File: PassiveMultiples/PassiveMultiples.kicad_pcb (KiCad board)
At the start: 2 copper layers, 15 x 100 mm, 9 parts, among them J1 AudioJack2_SwitchT, J2 AudioJack2_SwitchT, J3 AudioJack2_SwitchT, J4 AudioJack2_SwitchT, J5 AudioJack2_SwitchT, J6 AudioJack2_SwitchT, J7 AudioJack2_SwitchT, J8 AudioJack2_SwitchT, SW1 SW_Push_DPDT

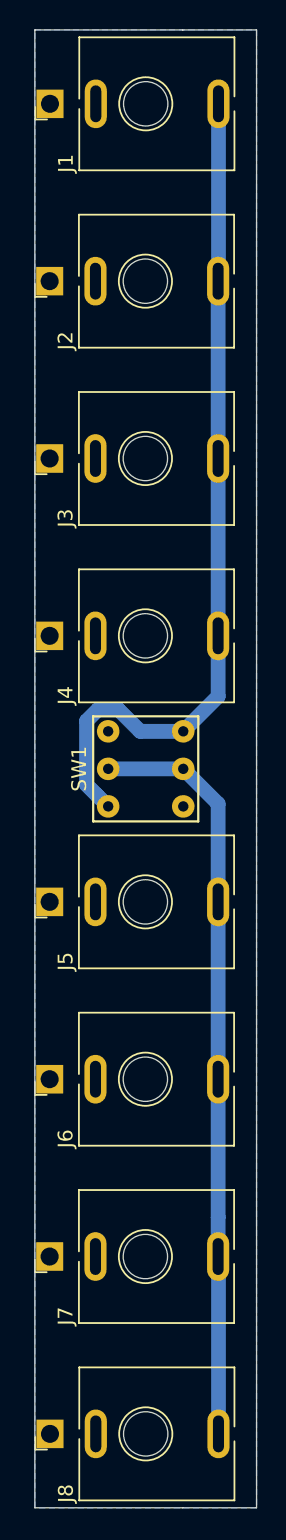
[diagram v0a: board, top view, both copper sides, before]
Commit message: Add top layer gnd pour
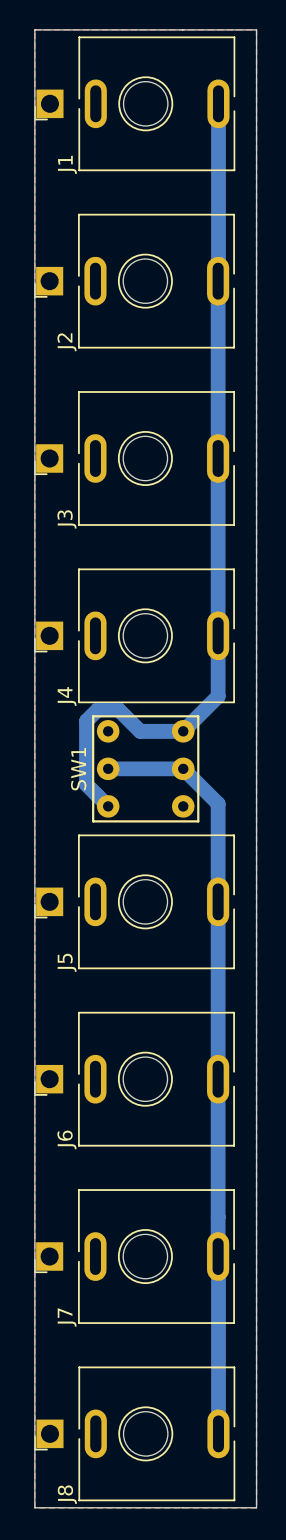
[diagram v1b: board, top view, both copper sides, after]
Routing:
- added copper zone on F.Cu, net Net-(J1-PadS)
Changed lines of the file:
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@@
   (layers
     (0 F.Cu signal)
-    (31 B.Cu signal hide)
+    (31 B.Cu signal)
     (32 B.Adhes user)
     (33 F.Adhes user)
@@
   )
   (setup
-    (last_trace_width 1)
+    (last_trace_width 0.25)
     (user_trace_width 0.2)
     (user_trace_width 0.25)
@@
     (solder_mask_min_width 0.25)
     (aux_axis_origin 0 0)
-    (visible_elements FFFFFF7F)
+    (visible_elements 7FFFFFFF)
     (pcbplotparams
       (layerselection 0x010fc_ffffffff)
@@
     (connect_pads (clearance 0.508))
     (min_thickness 0.254)
+    (fill yes (arc_segments 32) (thermal_gap 0.508) (thermal_bridge_width 0.508))
+    (polygon
+      (pts
+        (xy 150 40) (xy 165 40) (xy 165 140) (xy 150 140)
+      )
+    )
+  )
+  (zone (net 5) (net_name "Net-(J1-PadS)") (layer F.Cu) (hatch edge 0.508)
+    (connect_pads (clearance 0.508))
+    (min_thickness 0.254)

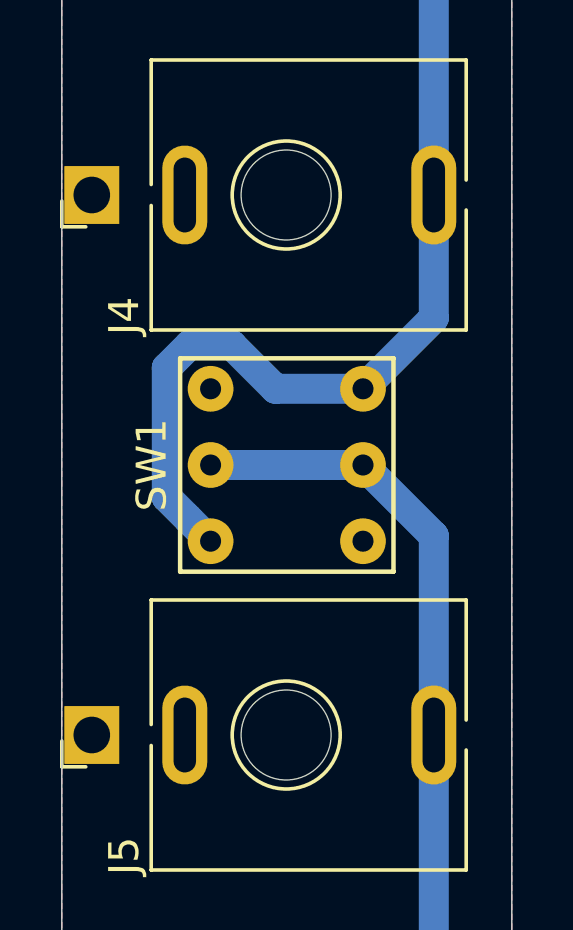
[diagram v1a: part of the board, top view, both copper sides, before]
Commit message: Update switch footprint
Generate gerbers and step
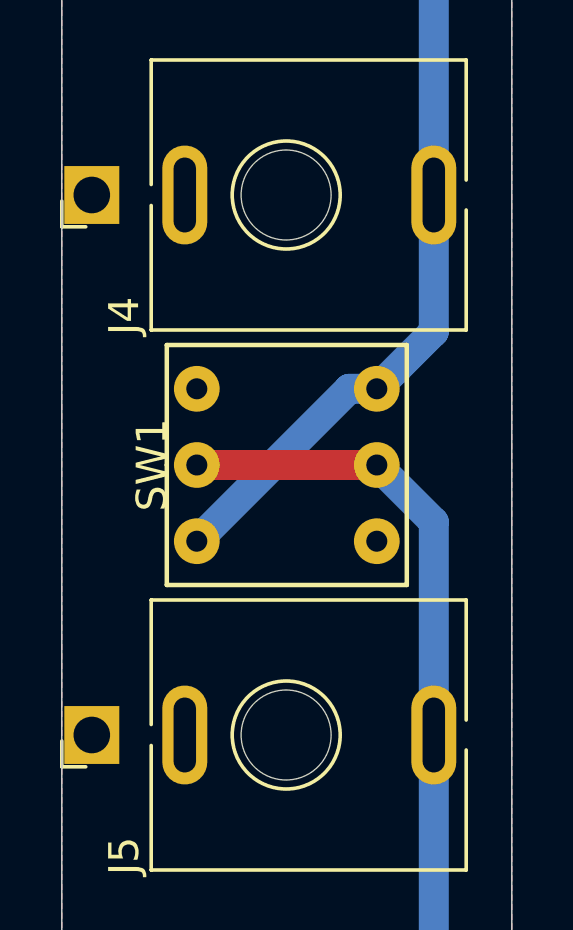
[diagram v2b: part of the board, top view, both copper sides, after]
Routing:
- net Net-(J1-PadT): track 57.3 -> 51.4 mm
- net Net-(J5-PadT): track 51.1 -> 51.8 mm
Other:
- board text added: "Passive Multiple v1.0"
- board text added: "schenktronics.com"

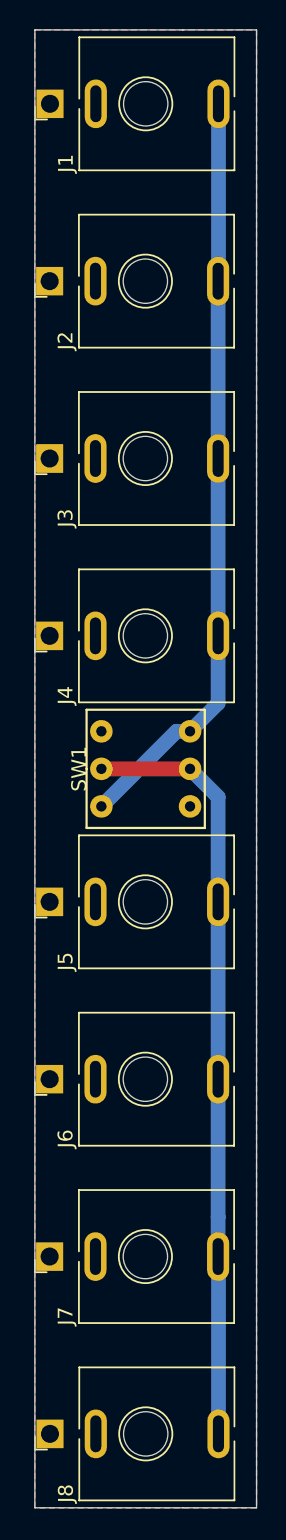
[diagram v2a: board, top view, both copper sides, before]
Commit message: Move jacks to try to center them
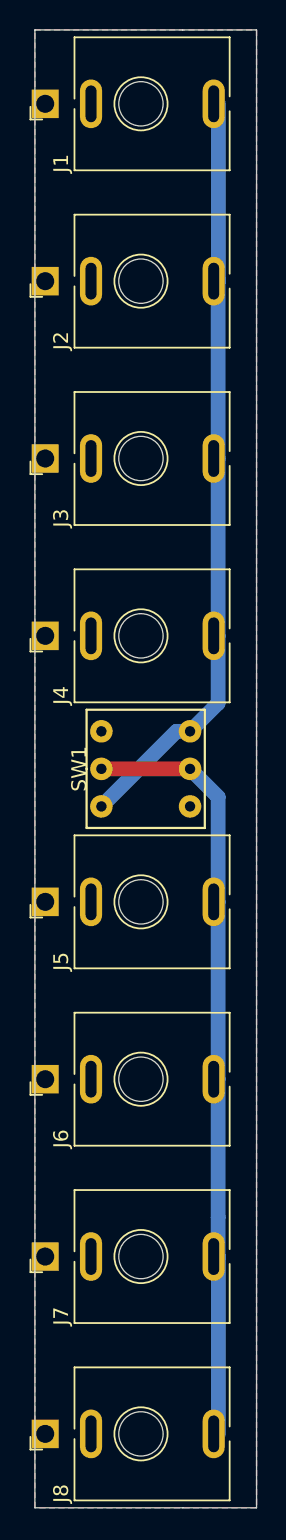
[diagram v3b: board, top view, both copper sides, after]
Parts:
- moved J1 0.32 mm to (150.7, 45.0)
- moved J8 0.32 mm to (150.7, 135.0)
- moved J2 0.30 mm to (150.7, 57.0)
- moved J3 0.30 mm to (150.7, 69.0)
- moved J4 0.30 mm to (150.7, 81.0)
- moved J5 0.30 mm to (150.7, 99.0)
- moved J6 0.30 mm to (150.7, 111.0)
- moved J7 0.30 mm to (150.7, 123.0)
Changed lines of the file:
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@@
   (page A4)
   (layers
-    (0 F.Cu signal)
-    (31 B.Cu signal)
+    (0 F.Cu signal hide)
+    (31 B.Cu signal hide)
     (32 B.Adhes user)
     (33 F.Adhes user)
@@
   )
   (setup
-    (last_trace_width 1)
+    (last_trace_width 0.25)
     (user_trace_width 0.2)
     (user_trace_width 0.25)
@@
   )
   (module _NTSFootprints:Jack_3.5mm_QingPu_WQP-PJ398SM_Vertical_CenterHole_OvalPads (layer F.Cu)
-    (at 151.023 45 90)
+    (at 150.7 45 90)
     (descr "TRS 3.5mm, vertical, Thonkiconn, PCB mount, (http://www.qingpu-electronics.com/en/products/WQP-PJ398SM-362.html)")
     (tags "WQP-PJ398SM WQP-PJ301M-12 TRS 3.5mm mono vertical jack thonkiconn qingpu")
@@
   )
   (module _NTSFootprints:Jack_3.5mm_QingPu_WQP-PJ398SM_Vertical_CenterHole_OvalPads (layer F.Cu)
-    (at 151 57 90)
+    (at 150.7 57 90)
     (descr "TRS 3.5mm, vertical, Thonkiconn, PCB mount, (http://www.qingpu-electronics.com/en/products/WQP-PJ398SM-362.html)")
     (tags "WQP-PJ398SM WQP-PJ301M-12 TRS 3.5mm mono vertical jack thonkiconn qingpu")
@@
   )
   (module _NTSFootprints:Jack_3.5mm_QingPu_WQP-PJ398SM_Vertical_CenterHole_OvalPads (layer F.Cu)
-    (at 151 69 90)
+    (at 150.7 69 90)
     (descr "TRS 3.5mm, vertical, Thonkiconn, PCB mount, (http://www.qingpu-electronics.com/en/products/WQP-PJ398SM-362.html)")
     (tags "WQP-PJ398SM WQP-PJ301M-12 TRS 3.5mm mono vertical jack thonkiconn qingpu")
@@
   )
   (module _NTSFootprints:Jack_3.5mm_QingPu_WQP-PJ398SM_Vertical_CenterHole_OvalPads (layer F.Cu)
-    (at 151 81 90)
+    (at 150.7 81 90)
     (descr "TRS 3.5mm, vertical, Thonkiconn, PCB mount, (http://www.qingpu-electronics.com/en/products/WQP-PJ398SM-362.html)")
     (tags "WQP-PJ398SM WQP-PJ301M-12 TRS 3.5mm mono vertical jack thonkiconn qingpu")
@@
   )
   (module _NTSFootprints:Jack_3.5mm_QingPu_WQP-PJ398SM_Vertical_CenterHole_OvalPads (layer F.Cu)
-    (at 151 99 90)
+    (at 150.7 99 90)
     (descr "TRS 3.5mm, vertical, Thonkiconn, PCB mount, (http://www.qingpu-electronics.com/en/products/WQP-PJ398SM-362.html)")
     (tags "WQP-PJ398SM WQP-PJ301M-12 TRS 3.5mm mono vertical jack thonkiconn qingpu")
@@
   )
   (module _NTSFootprints:Jack_3.5mm_QingPu_WQP-PJ398SM_Vertical_CenterHole_OvalPads (layer F.Cu)
-    (at 151 111 90)
+    (at 150.7 111 90)
     (descr "TRS 3.5mm, vertical, Thonkiconn, PCB mount, (http://www.qingpu-electronics.com/en/products/WQP-PJ398SM-362.html)")
     (tags "WQP-PJ398SM WQP-PJ301M-12 TRS 3.5mm mono vertical jack thonkiconn qingpu")
@@
   )
   (module _NTSFootprints:Jack_3.5mm_QingPu_WQP-PJ398SM_Vertical_CenterHole_OvalPads (layer F.Cu)
-    (at 151 123 90)
+    (at 150.7 123 90)
     (descr "TRS 3.5mm, vertical, Thonkiconn, PCB mount, (http://www.qingpu-electronics.com/en/products/WQP-PJ398SM-362.html)")
     (tags "WQP-PJ398SM WQP-PJ301M-12 TRS 3.5mm mono vertical jack thonkiconn qingpu")
@@
   )
   (module _NTSFootprints:Jack_3.5mm_QingPu_WQP-PJ398SM_Vertical_CenterHole_OvalPads (layer F.Cu)
-    (at 151.023 135 90)
-    (descr "TRS 3.5mm, vertical, Thonkiconn, PCB mount, (http://www.qingpu-electronics.com/en/products/WQP-PJ398SM-362.html)")
-    (tags "WQP-PJ398SM WQP-PJ301M-12 TRS 3.5mm mono vertical jack thonkiconn qingpu")
+    (at 150.7 135 90)
+    (descr "TRS 3.5mm, vertical, Thonkiconn, PCB mount, (http://www.qingpu-electronics.com/en/products/WQP-PJ398SM-362.html)")
+    (tags "WQP-PJ398SM WQP-PJ301M-12 TRS 3.5mm mono vertical jack thonkiconn qingpu")
